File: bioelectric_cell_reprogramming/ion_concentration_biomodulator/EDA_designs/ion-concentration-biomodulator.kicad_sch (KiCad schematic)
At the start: 36 parts, among them J1 Conn_01x06_Pin, J10 39-53-2045, J11 Conn_01x14_Pin, J12 Conn_01x14_Pin, J13 39-53-2045, J14 39-53-2045, J15 Conn_ARM_SWD_TagConnect_TC2030, J16 Conn_01x02_Socket, J18 EJ508A, J2 Conn_01x06_Pin, J3 Conn_01x06_Pin, J4 Conn_01x06_Pin, J8 39-53-2045, Q1 CSD16327Q3, Q2 CSD16327Q3, SW2 SW_Nidec_CAS-120A1, U1 LM2576HVS-3.3, U2 SCD41-D-R2, U4 LM2576HVS-5, U6 STM32F410C8Tx

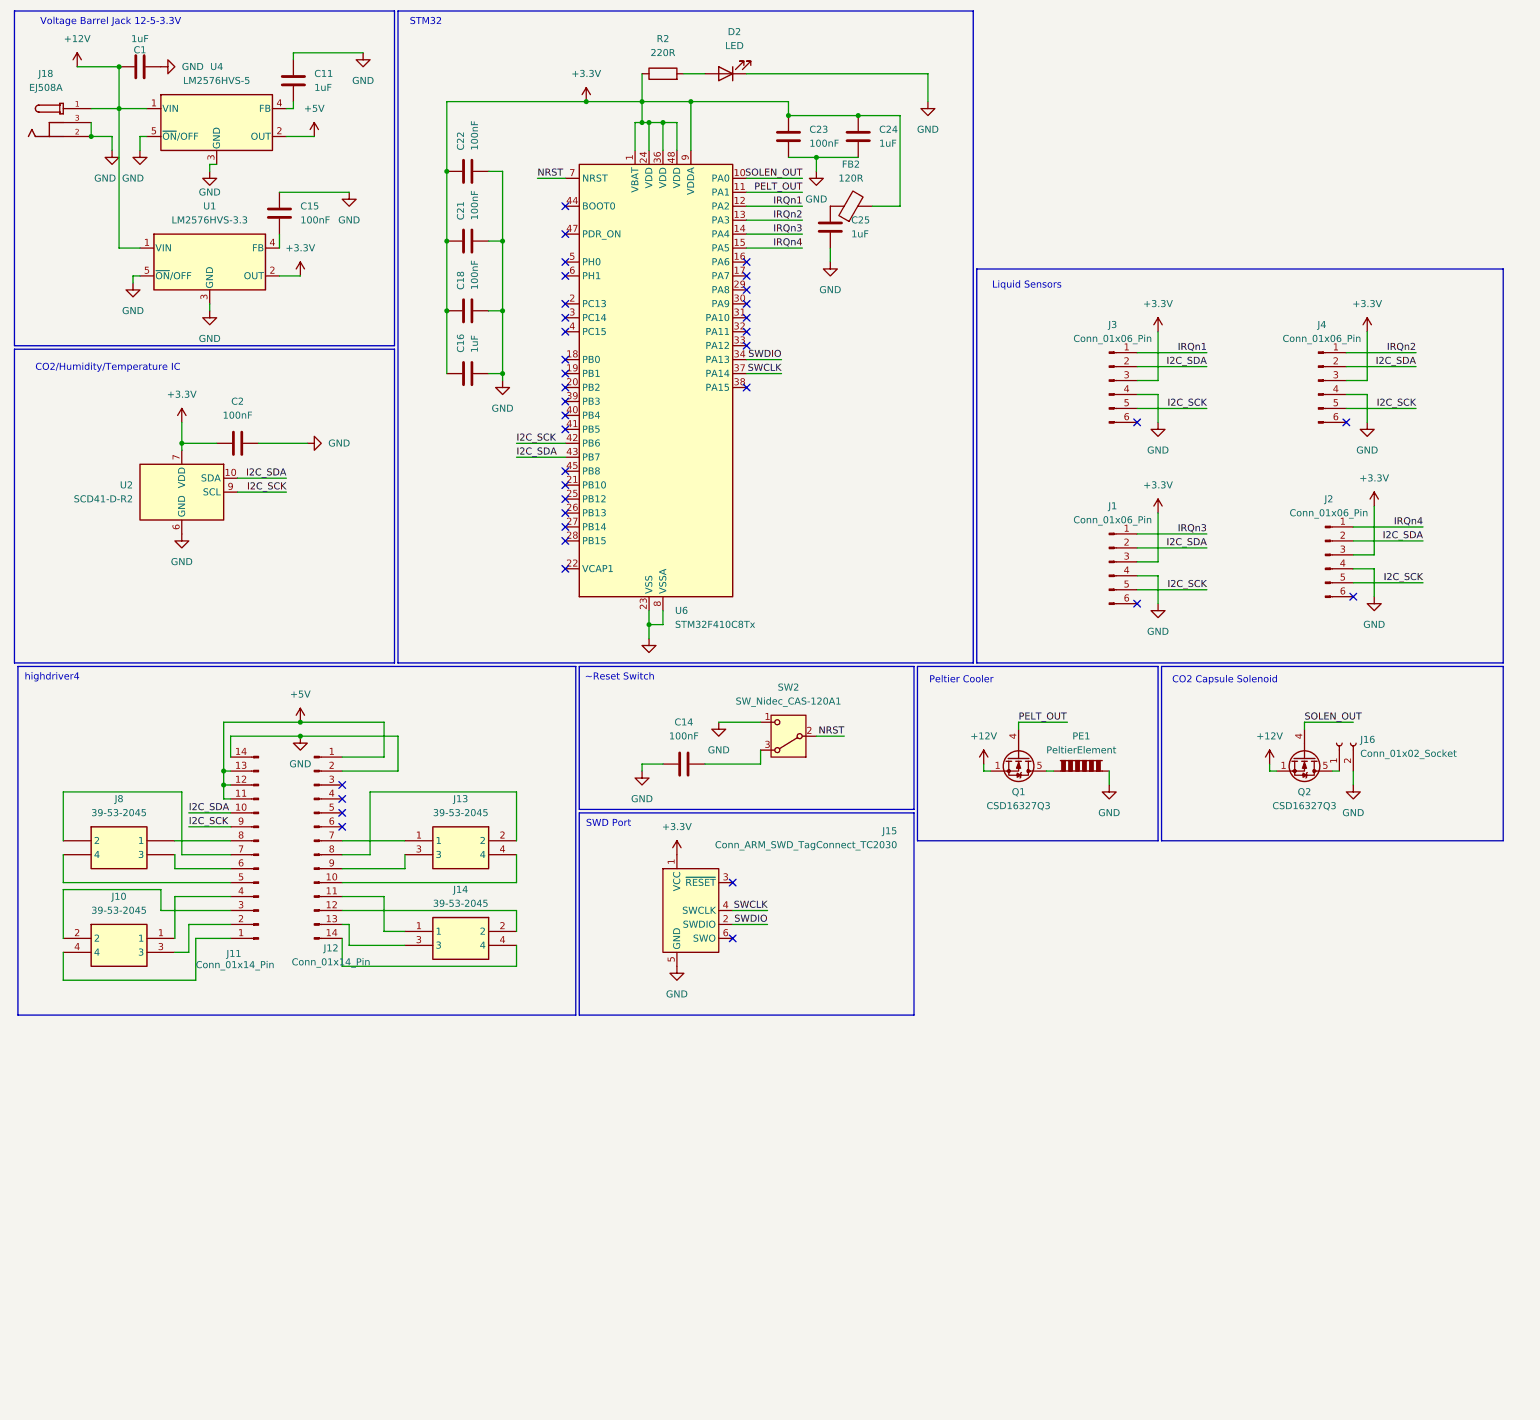
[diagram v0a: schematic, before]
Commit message: refactor: added project-specific subdirectories, added ion concentration biomodulato
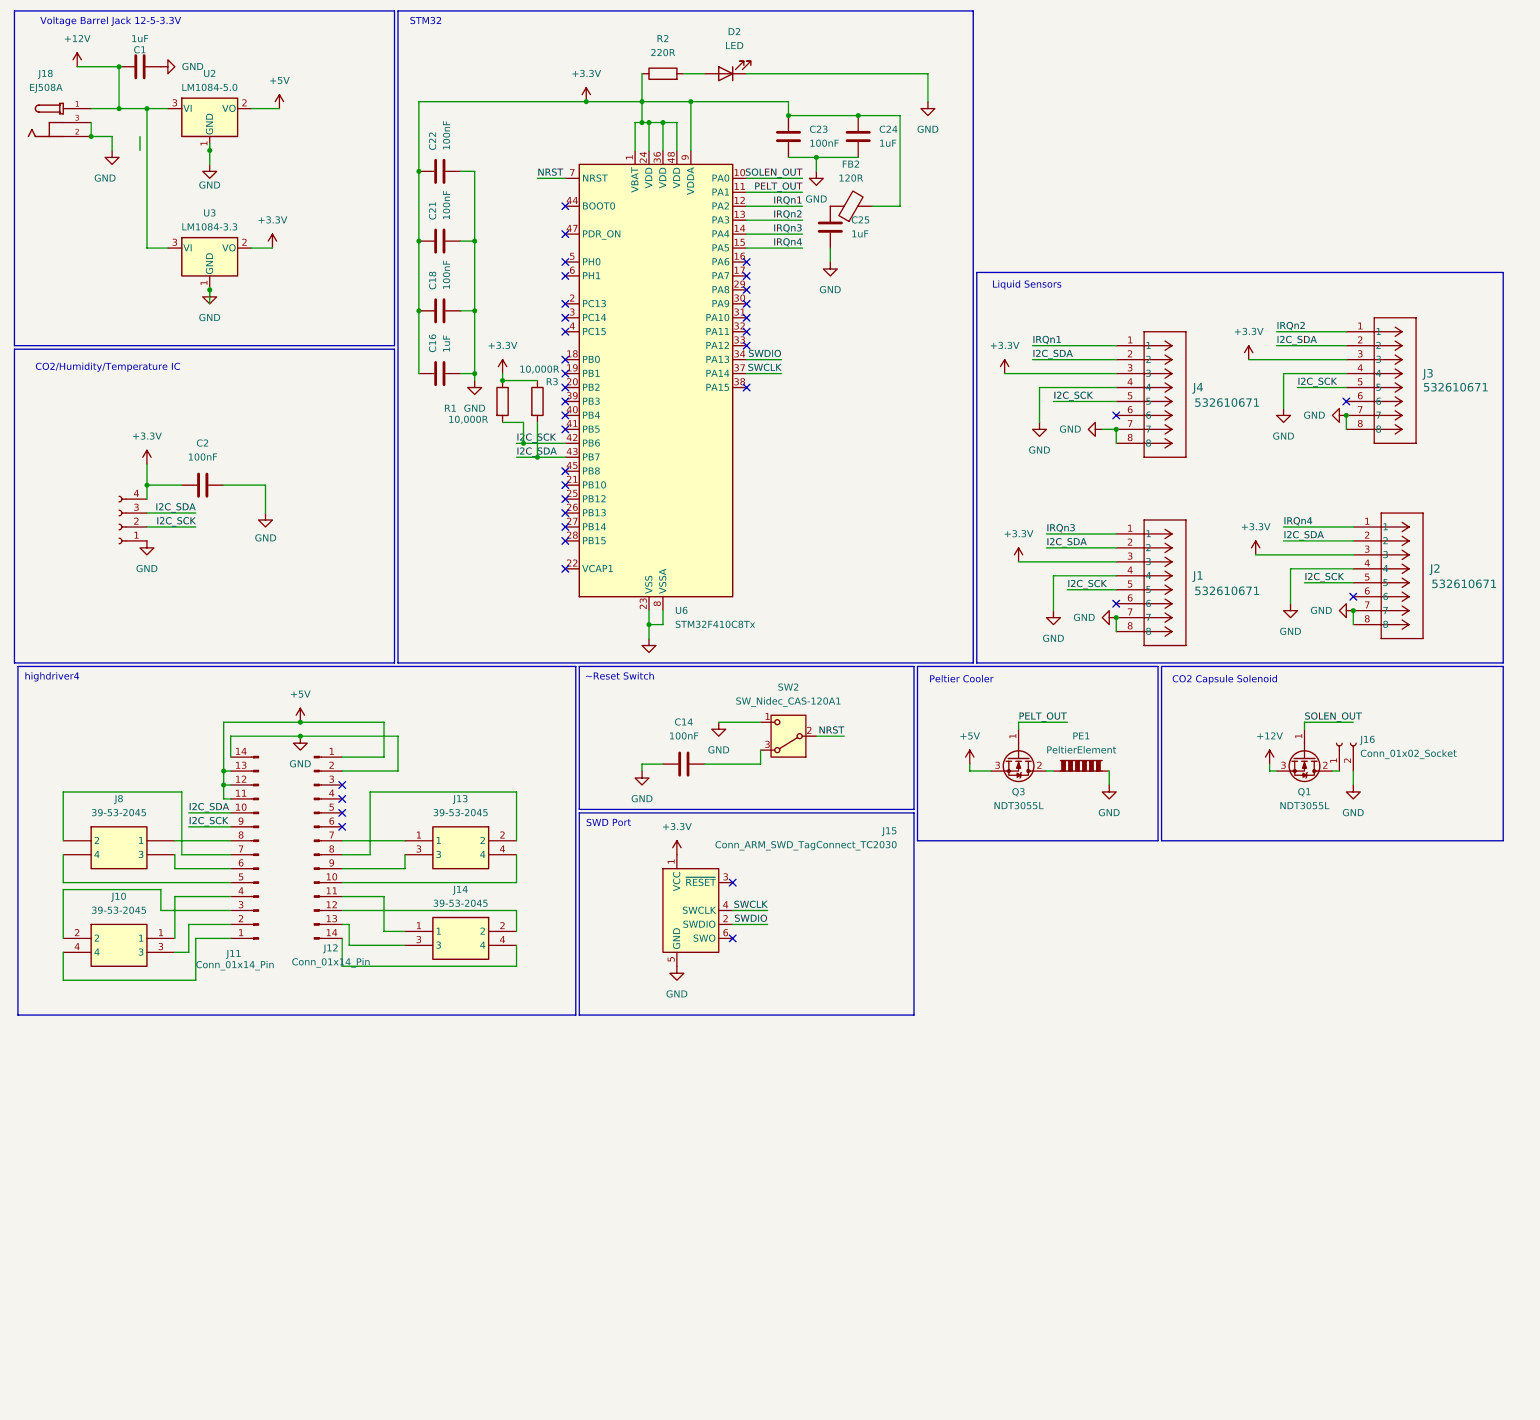
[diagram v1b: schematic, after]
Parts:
- removed C11: 1uF, Capacitor_SMD:C_0402_1005Metric, symbol Device:C
- removed C15: 100nF, Capacitor_SMD:C_0402_1005Metric, symbol Device:C
- removed J1, J2, J3, J4: Conn_01x06_Pin, Connector_Hirose:Hirose_DF13-06P-1.25DSA_1x06_P1.25mm_Vertical, symbol Connector:Conn_01x06_Pin
- removed Q1, Q2: CSD16327Q3, Package_SON:VSON-8_3.3x3.3mm_P0.65mm_NexFET, symbol Transistor_FET:CSD16327Q3
- removed U1: LM2576HVS-3.3, Package_TO_SOT_SMD:TO-263-5_TabPin3, symbol Regulator_Switching:LM2576HVS-3.3
- removed U2: SCD41-D-R2, Sensor:Sensirion_SCD4x-1EP_10.1x10.1mm_P1.25mm_EP4.8x4.8mm, symbol Sensor_Gas:SCD41-D-R2
- removed U4: LM2576HVS-5, Package_TO_SOT_SMD:TO-263-5_TabPin3, symbol Regulator_Switching:LM2576HVS-5
- added J1, J2, J3, J4: 532610671, co2_sensor_footprint:CON_532610671, symbol co2_sensor_molex_footprint:532610671
- added J5: Conn_01x04_Socket, Connector_PinSocket_2.54mm:PinSocket_1x04_P2.54mm_Vertical, symbol Connector:Conn_01x04_Socket
- added Q1, Q3: NDT3055L, Package_TO_SOT_SMD:SOT-223-3_TabPin2, symbol Transistor_FET:NDT3055L
- added R1, R3: 10,000R, Resistor_THT:R_Axial_DIN0207_L6.3mm_D2.5mm_P7.62mm_Horizontal, symbol Device:R
- added U2: LM1084-5.0, lm1084IT_regulator:T03B, symbol Regulator_Linear:LM1084-5.0
- added U3: LM1084-3.3, lm1084IT_regulator:T03B, symbol Regulator_Linear:LM1084-3.3
- FB2: footprint Inductor_SMD:L_7.3x7.3_H4.5 -> Inductor_SMD:L_0603_1608Metric
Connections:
- net +12V: now also Q1.3 (S), U2.3 (VI), U3.3 (VI)
- net +3.3V: now also J1.3, J2.3, J3.3, J4.3, J5.4 (Pin_4), R1.1, R3.1, U3.2 (VO)
- net +5V: now also Q3.3 (S), U2.2 (VO)
- net GND: now also J1.4, J1.7, J1.8, J2.4, J2.7, J2.8, J3.4, J3.7, J3.8, J4.4, J4.7, J4.8, J5.1 (Pin_1), U2.1 (GND), U3.1 (GND)
- net I2C_SCK: now also J1.5, J2.5, J3.5, J4.5, J5.2 (Pin_2), R1.2
- net I2C_SDA: now also J1.2, J2.2, J3.2, J4.2, J5.3 (Pin_3), R3.2
- net IRQn1: now also J4.1
- net IRQn2: now also J3.1
- net IRQn3: now also J1.1
- net IRQn4: now also J2.1
- net PELT_OUT: now also Q3.1 (G)
- net SOLEN_OUT: now also Q1.1 (G)
- net at J16.1 (Pin_1): now also Q1.2 (D)
- net at PE1.1: now also Q3.2 (D)
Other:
- moved on the sheet: C16, C18, C2, C21, C22

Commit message: pushing v6
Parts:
- removed C2: 100nF, Capacitor_SMD:C_0402_1005Metric, symbol Device:C
- removed J16: Conn_01x02_Socket, Connector_PinSocket_2.54mm:PinSocket_1x02_P2.54mm_Vertical, symbol Connector:Conn_01x02_Socket
- removed J5: Conn_01x04_Socket, Connector_PinSocket_2.54mm:PinSocket_1x04_P2.54mm_Vertical, symbol Connector:Conn_01x04_Socket
- removed PE1: PeltierElement, Connector_PinSocket_2.54mm:PinSocket_1x02_P2.54mm_Vertical, symbol Device:PeltierElement
- removed U6: STM32F410C8Tx, Package_QFP:LQFP-48_7x7mm_P0.5mm, symbol MCU_ST_STM32F4:STM32F410C8Tx
- added C3: 100nF, Capacitor_SMD:C_0402_1005Metric, symbol Device:C
- added J16: IPL1-104-01-L-D-K, pinch_solenoid:CONN_IPL1-104-01-x-D-x_SAI, symbol 1x08_connector_pinch_solenoid:IPL1-104-01-L-D-K
- added J17, J6: Conn_01x02_Pin, Connector_PinHeader_2.00mm:PinHeader_1x02_P2.00mm_Vertical, symbol Connector:Conn_01x02_Pin
- added J5: S4B-PH-SM4-TB, co2_dev_board_male_socket:CONN4_S4B-PH-SM4-TB_JST, symbol co2_dev_board_male_socket:S4B-PH-SM4-TB
- added J7: 6620XX11122_66200211122, peltier_cooler_socket_footprint:66200211122, symbol 1x02_connector_peltier:6620XX11122_66200211122
- added J9: IPL1-102-01-L-S-K, solenoid_footprint:CONN_IPL1-102-01-L-S-K_SAI, symbol 1x02_connector_solenoid:IPL1-102-01-L-S-K
- added Q2, Q4, Q5, Q6: NDT3055L, Package_TO_SOT_SMD:SOT-223-3_TabPin2, symbol Transistor_FET:NDT3055L
- added U1: STM32F410CBTx, Package_QFP:LQFP-48_7x7mm_P0.5mm, symbol MCU_ST_STM32F4:STM32F410CBTx
- U2, U3: footprint lm1084IT_regulator:T03B -> LDO_5V:T03B
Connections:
- net +12V: now also Q2.3 (S), Q4.3 (S), Q5.3 (S), Q6.3 (S)
- net +3.3V: now also C3.1, J5.3, U1.1 (VBAT), U1.24 (VDD), U1.36 (VDD), U1.48 (VDD), U1.9 (VDDA)
- net GND: now also C3.2, J16.2, J16.4, J16.6, J16.8, J5.2, J7.2, J9.2, U1.23 (VSS), U1.35 (VSS), U1.46 (VSS), U1.8 (VSSA)
- net I2C_SCK: now also J5.1, U1.42 (PB6)
- net I2C_SDA: now also J5.4, U1.43 (PB7)
- net IRQn1: now also U1.12 (PA2)
- net IRQn2: now also U1.13 (PA3)
- net IRQn3: now also U1.14 (PA4)
- net IRQn4: now also U1.15 (PA5)
- net NRST: now also J6.1 (Pin_1), U1.7 (NRST)
- net PELT_OUT: now also U1.11 (PA1)
- net SOLEN_OUT: now also U1.10 (PA0)
- net SWCLK: now also U1.37 (PA14)
- net SWDIO: now also U1.34 (PA13)
- net at J15.3 (~{RESET}): now also J6.2 (Pin_2)
- net at J15.6 (SWO): now also J17.2 (Pin_2)
- net at Q3.2 (D): now also J7.1
- net at Q1.2 (D): now also J9.1
- new net: J16.1, Q2.2 (D)
- new net: J16.3, Q4.2 (D)
- new net: J16.5, Q5.2 (D)
- new net: J16.7, Q6.2 (D)
- new net SOL1: Q2.1 (G), U1.16 (PA6)
- new net SOL2: Q4.1 (G), U1.17 (PA7)
- new net SOL3: Q5.1 (G), U1.29 (PA8)
- new net SOL4: Q6.1 (G), U1.30 (PA9)
- new net SWO: J17.1 (Pin_1), U1.39 (PB3)
- no-connect marks 38 -> 31
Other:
- note added: "11+"
- note added: "11-"
- note added: "12+"
- note added: "12-"
- note added: "21+"
- note added: "21-"
- note added: "22+"
- note added: "22-"
- note added: "31+"
- note added: "31-"
- note added: "32+"
- note added: "32-"
- note added: "41+"
- note added: "41-"
- note added: "42+"
- note added: "42-"
- note added: "5V"
- note added: "A0"
- note added: "A1"
- note added: "GND"
- note added: "SCL"
- note added: "SDA"
- moved on the sheet: J1, J12, J2, J3, J4

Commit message: pushing v7
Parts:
- D2: footprint LED_THT:LED_D3.0mm -> LED_THT:LED_D1.8mm_W1.8mm_H2.4mm_Horizontal_O3.81mm_Z1.6mm
- R1, R3: footprint Resistor_THT:R_Axial_DIN0207_L6.3mm_D2.5mm_P7.62mm_Horizontal -> Resistor_SMD:R_01005_0402Metric
- R2: footprint Resistor_THT:R_Axial_DIN0204_L3.6mm_D1.6mm_P5.08mm_Horizontal -> Resistor_SMD:R_01005_0402Metric
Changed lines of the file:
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@@
 			)
 		)
-		(property "Footprint" "LED_THT:LED_D3.0mm"
+		(property "Footprint" "LED_THT:LED_D1.8mm_W1.8mm_H2.4mm_Horizontal_O3.81mm_Z1.6mm"
 			(at 142.24 25.4 0)
 			(effects
@@
 			)
 		)
-		(property "Footprint" "Resistor_THT:R_Axial_DIN0204_L3.6mm_D1.6mm_P5.08mm_Horizontal"
+		(property "Footprint" "Resistor_SMD:R_01005_0402Metric"
 			(at 130.81 27.178 90)
 			(effects
@@
 			)
 		)
-		(property "Footprint" "Resistor_THT:R_Axial_DIN0207_L6.3mm_D2.5mm_P7.62mm_Horizontal"
+		(property "Footprint" "Resistor_SMD:R_01005_0402Metric"
 			(at 106.172 85.09 90)
 			(effects
@@
 			)
 		)
-		(property "Footprint" "Resistor_THT:R_Axial_DIN0207_L6.3mm_D2.5mm_P7.62mm_Horizontal"
+		(property "Footprint" "Resistor_SMD:R_01005_0402Metric"
 			(at 99.822 85.09 90)
 			(effects

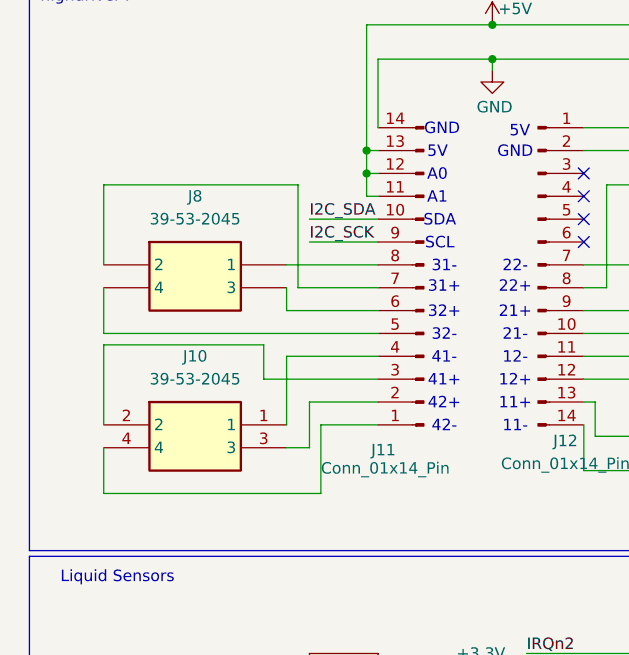
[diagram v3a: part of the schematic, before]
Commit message: fix: left-sided highdriver4 pinout (schematic)
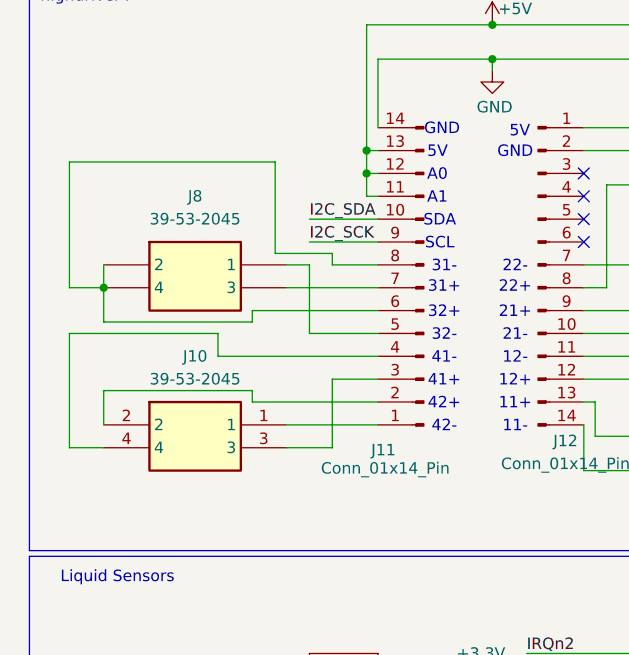
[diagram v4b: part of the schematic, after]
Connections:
- net at J8.1: now also J11.5 (Pin_5); no longer J11.8 (Pin_8)
- net at J8.2: now also J11.6 (Pin_6), J11.8 (Pin_8), J8.4; no longer J11.7 (Pin_7)
- net at J8.3: now also J11.7 (Pin_7); no longer J11.6 (Pin_6)
- net at J10.1: now also J11.1 (Pin_1); no longer J11.4 (Pin_4)
- net at J10.2: now also J11.2 (Pin_2); no longer J11.3 (Pin_3)
- net at J10.3: now also J11.3 (Pin_3); no longer J11.2 (Pin_2)
- net at J10.4: now also J11.4 (Pin_4); no longer J11.1 (Pin_1)

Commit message: pushing minor v7 changes
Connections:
- net at J11.6 (Pin_6), J8.2: no longer J11.8 (Pin_8), J8.4
- new net: J11.8 (Pin_8), J8.4
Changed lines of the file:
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@@
-	)
-	(junction
-		(at 21.59 167.64)
-		(diameter 0)
-		(color 0 0 0 0)
 	)
 	(junction
@@
 	(wire
 		(pts
-			(xy 21.59 167.64) (xy 21.59 165.1)
-		)
-		(stroke
-			(width 0)
-			(type default)
-		)
-	)
-	(wire
-		(pts
 			(xy 200.66 152.4) (xy 205.74 152.4)
 		)
@@
 	(wire
 		(pts
-			(xy 21.59 171.45) (xy 21.59 167.64)
-		)
-		(stroke
-			(width 0)
-			(type default)
-		)
-	)
-	(wire
-		(pts
 			(xy 96.52 43.18) (xy 93.98 43.18)
 		)
@@
 	(wire
 		(pts
+			(xy 19.05 165.1) (xy 19.05 171.45)
+		)
+		(stroke
+			(width 0)
+			(type default)
+		)
+	)
+	(wire
+		(pts
 			(xy 34.29 172.72) (xy 17.78 172.72)
 		)
@@
 	(wire
 		(pts
-			(xy 38.1 171.45) (xy 21.59 171.45)
+			(xy 38.1 171.45) (xy 19.05 171.45)
 		)
 		(stroke
@@
 		)
 		(stroke
+			(width 0)
+			(type default)
+		)
+	)
+	(wire
+		(pts
+			(xy 19.05 165.1) (xy 21.59 165.1)
+		)
+		(stroke

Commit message: pushing v7
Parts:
- removed C14: 100nF, Capacitor_SMD:C_0402_1005Metric, symbol Device:C
- removed SW2: SW_Nidec_CAS-120A1, Button_Switch_SMD:Nidec_Copal_CAS-120A, symbol Switch:SW_Nidec_CAS-120A1
- added C2: 100nF, Capacitor_SMD:C_0402_1005Metric, symbol Device:C
- added F1: Fuse, Fuse:Fuse_0603_1608Metric, symbol Device:Fuse
- added J19: USB_C_Receptacle_USB2.0_14P, Connector_USB:USB_C_Receptacle_GCT_USB4105-xx-A_16P_TopMnt_Horizontal, symbol Connector:USB_C_Receptacle_USB2.0_14P
- added R4, R5: 5,100R, Resistor_SMD:R_0603_1608Metric, symbol Device:R
- added SW1: SW_Push, Button_Switch_THT:SW_PUSH-12mm_Wuerth-430476085716, symbol Switch:SW_Push
- added U4: USBLC6-2SC6, Package_TO_SOT_SMD:SOT-23-6, symbol Power_Protection:USBLC6-2SC6
- C1: footprint Capacitor_SMD:C_0402_1005Metric -> Capacitor_SMD:C_1812_4532Metric
- D2: footprint LED_THT:LED_D1.8mm_W1.8mm_H2.4mm_Horizontal_O3.81mm_Z1.6mm -> LED_SMD:LED_0201_0603Metric
- R1, R2, R3: footprint Resistor_SMD:R_01005_0402Metric -> Resistor_SMD:R_0201_0603Metric
- U2, U3: footprint LDO_5V:T03B -> LDO_5V:TS3B
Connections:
- net +5V: now also F1.2, U4.5 (VBUS)
- net GND: now also C2.2, J19.A1 (GND), J19.A12 (GND), J19.B1 (GND), J19.B12 (GND), J19.S1 (SHIELD), R4.2, R5.2, SW1.1, U4.2 (GND)
- net NRST: now also C2.1, SW1.2
- net SOL3: now also U1.18 (PB0); no longer U1.29 (PA8)
- net SOL4: now also U1.19 (PB1); no longer U1.30 (PA9)
- net USART1_RX: now reaches U1.31 (PA10)
- net D-: now reaches U1.32 (PA11)
- net D-: now also U4.6 (I/O1)
- net D+: now reaches U1.33 (PA12)
- net D+: now also U4.4 (I/O2)
- net 21+: now reaches J12.9 (Pin_9), J13.3
- net 21-: now reaches J12.10 (Pin_10), J13.4
- net 32-: now reaches J11.5 (Pin_5), J8.1
- net 32+: now reaches J11.6 (Pin_6), J8.2
- net 31+: now reaches J11.7 (Pin_7), J8.3
- net 31-: now reaches J11.8 (Pin_8), J8.4
- net 42-: now reaches J10.1, J11.1 (Pin_1)
- net 42+: now reaches J10.2, J11.2 (Pin_2)
- net 41+: now reaches J10.3, J11.3 (Pin_3)
- net 41-: now reaches J10.4, J11.4 (Pin_4)
- net 12-: now reaches J12.11 (Pin_11), J14.1
- net 12+: now reaches J12.12 (Pin_12), J14.2
- net 11+: now reaches J12.13 (Pin_13), J14.3
- net 11-: now reaches J12.14 (Pin_14), J14.4
- new net: F1.1, J19.A4 (VBUS), J19.A9 (VBUS), J19.B4 (VBUS), J19.B9 (VBUS)
- new net: J19.A7 (D-), J19.B7 (D-), U4.1 (I/O1)
- new net: J19.A6 (D+), J19.B6 (D+), U4.3 (I/O2)
- new net: J19.A5 (CC1), R4.1
- new net: J19.B5 (CC2), R5.1
- new net USART1_TX: U1.30 (PA9)
- no-connect marks 31 -> 27
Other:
- moved on the sheet: C16, C18, C21, C22, C23, C24, C25, D2, FB2, R1, R2, R3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

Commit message: finished v7 (cleared by DRC)
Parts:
- F1: value Fuse -> 500mA
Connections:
- net USART1_RX: no longer names the net of U1.31 (PA10)
- net USART1_TX: no longer names the net of U1.30 (PA9)
- no-connect marks 27 -> 29
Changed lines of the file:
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@@
 	)
 	(no_connect
+		(at 149.86 67.31)
+	)
+	(no_connect
 		(at 116.84 87.63)
 	)
@@
 	)
 	(no_connect
+		(at 149.86 69.85)
+	)
+	(no_connect
 		(at 82.55 256.54)
 	)
@@
 	(wire
 		(pts
-			(xy 160.02 67.31) (xy 149.86 67.31)
-		)
-		(stroke
-			(width 0)
-			(type default)
-		)
-	)
-	(wire
-		(pts
 			(xy 74.93 152.4) (xy 82.55 152.4)
 		)
@@
 	(wire
 		(pts
-			(xy 161.29 69.85) (xy 149.86 69.85)
-		)
-		(stroke
-			(width 0)
-			(type default)
-		)
-	)
-	(wire
-		(pts
 			(xy 90.17 58.42) (xy 90.17 45.72)
 		)
@@
 		)
 	)
-	(label "USART1_TX"
-		(at 160.02 67.31 180)
-		(fields_autoplaced yes)
-		(effects
-			(font
-				(size 1.27 1.27)
-			)
-			(justify right bottom)
-		)
-	)
 	(label "11+"
 		(at 74.93 180.34 0)
@@
 		)
 	)
-	(label "USART1_RX"
-		(at 161.29 69.85 180)
-		(fields_autoplaced yes)
-		(effects
-			(font
-				(size 1.27 1.27)
-			)
-			(justify right bottom)
-		)
-	)
 	(label "I2C_SCK"
 		(at 107.95 92.71 0)
@@
 			)
 		)
-		(property "Value" "Fuse"
+		(property "Value" "500mA"
 			(at 256.54 88.9 90)
 			(effects
